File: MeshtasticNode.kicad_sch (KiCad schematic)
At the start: 38 parts, among them J1 Conn_01x02_Socket, J2 Conn_01x02_Socket, J3 Conn_01x04_Socket, J4 Conn_01x03_Pin, J5 Conn_01x03_Pin, J6 Conn_01x03_Pin, J8 Conn_01x03_Pin, U1 BQ24074, U2 HT-CT62, U8 XC6206PxxxMR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

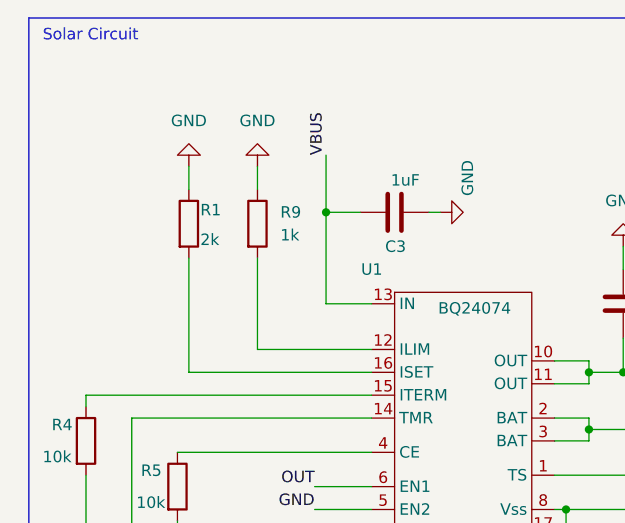
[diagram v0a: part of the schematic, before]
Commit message: Increase maximum current from 500mA to 2A
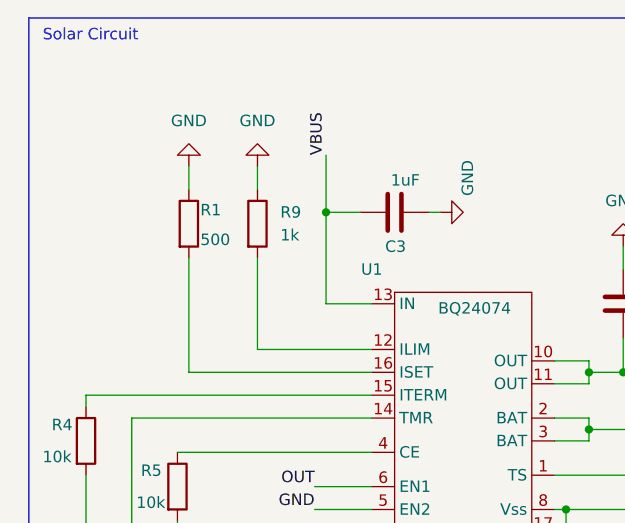
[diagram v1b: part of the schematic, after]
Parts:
- R1: value 2k -> 500
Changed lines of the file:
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@@
 			)
 		)
-		(property "Value" "2k"
+		(property "Value" "500"
 			(at 31.75 37.338 0)
 			(effects

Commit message: pcb: Make EN1 and EN2 selectable. Fixes awful bug.
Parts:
- removed TP1: TestPoint, Connector_PinHeader_2.54mm:PinHeader_1x01_P2.54mm_Vertical, symbol Connector:TestPoint
- added JP1, JP2: SolderJumper_3_Open, Jumper:SolderJumper-3_P1.3mm_Open_RoundedPad1.0x1.5mm_NumberLabels, symbol Jumper:SolderJumper_3_Open
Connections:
- net GND: now also JP1.1 (A), JP2.1 (A); no longer U1.5 (EN2)
- net OUT: now also JP1.3 (B), JP2.3 (B); no longer U1.6 (EN1)
- new net EN1: JP1.2 (C), U1.6 (EN1)
- new net EN2: JP2.2 (C), U1.5 (EN2)

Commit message: pcb: add I2C port and remove a few warnings from EN1/EN2 solder switches
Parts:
- added J7: Conn_01x04_Socket, Connector_JST:JST_PH_B4B-PH-K_1x04_P2.00mm_Vertical, symbol Connector:Conn_01x04_Socket
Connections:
- net +3V3: now also J7.2 (Pin_2)
- net GND: now also J7.1 (Pin_1)
- net USB_D+ renamed I2C_SDA
- net I2C_SDA: now also J7.3 (Pin_3)
- net USB_D- renamed I2C_SCL
- net I2C_SCL: now also J7.4 (Pin_4)
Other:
- note added: "I2C"
- moved on the sheet: H3

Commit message: pcb: add lost front and back groundplane, use thermal via footprint for BQ24074
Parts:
- U1: footprint Package_DFN_QFN:VQFN-16-1EP_3x3mm_P0.5mm_EP1.68x1.68mm -> Package_DFN_QFN:VQFN-16-1EP_3x3mm_P0.5mm_EP1.68x1.68mm_ThermalVias
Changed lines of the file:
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@@
 			)
 		)
-		(property "Footprint" "Package_DFN_QFN:VQFN-16-1EP_3x3mm_P0.5mm_EP1.68x1.68mm"
+		(property "Footprint" "Package_DFN_QFN:VQFN-16-1EP_3x3mm_P0.5mm_EP1.68x1.68mm_ThermalVias"
 			(at 50.8 40.64 0)
 			(effects
